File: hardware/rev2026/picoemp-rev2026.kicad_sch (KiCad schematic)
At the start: 53 parts, among them J1 EDGE-SMA, J2 1x2_Pin_Header, J3 MKDS 1,5/2-5.08, J4 EDGE-SMA, P1 Header 7, P2 Header 2, P3 Header 4, Q1 LDA111STR, Q2 RGT16BM65DTL, Q3 AO3422, Q4 AO3422, SW1 KSC741J LFS, SW2 KSC741J LFS, SW3 TL3301AF160QJ, T1 ATB322524, T2 ATB322524, U1 SC0915, U2 74LVC1G17

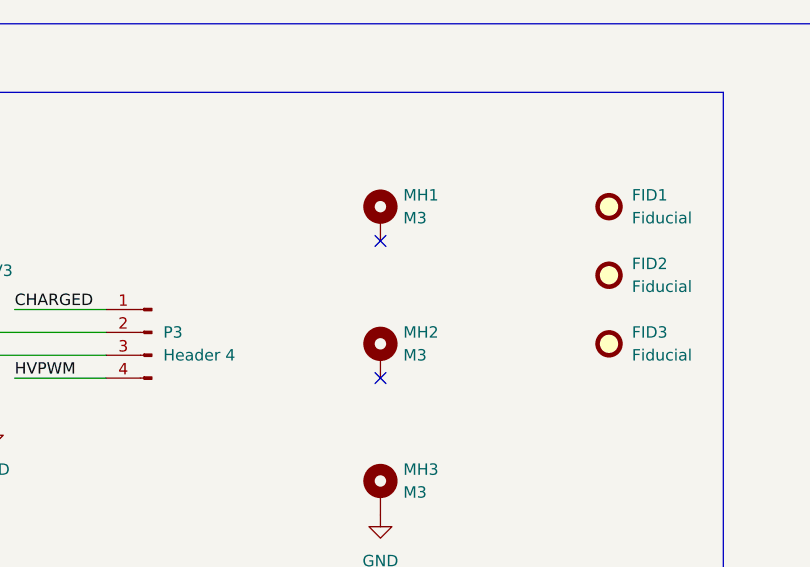
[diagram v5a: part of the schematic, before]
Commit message: MH1/MH2 to bare non-plated holes; HV_OUT reroute
MH1 and MH2 are now MountingHole_3.2mm_M3 as np_thru_hole -- no copper at all.
That removes two 6.4 mm floating pads from beside a 250 V node, and with them the
tightest barrier gap on the board: /HV_GATE was running 1.060 mm from MH1's pad.
The limit is now the transformers again at 1.135 mm. MH3 keeps its plated pad;
it sits at the logic end where floating copper is not a concern.

HV_OUT rerouted: 51.9 -> 22.2 mm. Discharge loop total 162.5 -> 131.5 mm.

Still open: one dangling via at (122.20, 147.20), B.Cu only, and J1's left shield
tab at (120.14, 147.2417) is not connected to copper. Electrically the shield is
one piece through the connector body, but DRC counts the islands.

Co-Authored-By: Claude Opus 5 <noreply@anthropic.com>
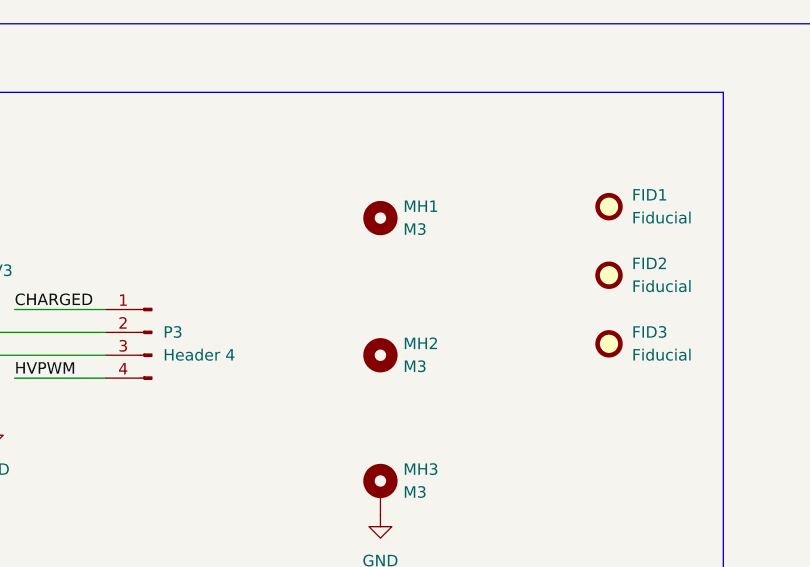
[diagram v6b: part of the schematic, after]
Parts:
- MH1, MH2: footprint MountingHole:MountingHole_3.2mm_M3_Pad_Via -> MountingHole:MountingHole_3.2mm_M3; symbol Mechanical:MountingHole_Pad -> Mechanical:MountingHole
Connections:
- no-connect marks 26 -> 24
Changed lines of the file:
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@@
 	)
 	(no_connect
-		(at 123.19 198.12)
-	)
-	(no_connect
 		(at 119.38 139.7)
 	)
 	(no_connect
-		(at 123.19 213.36)
-	)
-	(no_connect
 		(at 119.38 124.46)
 	)
@@
 	)
 	(symbol
-		(lib_id "Mechanical:MountingHole_Pad")
+		(lib_id "Mechanical:MountingHole")
 		(at 123.19 210.82 0)
 		(unit 1)
@@
 		(fields_autoplaced yes)
 		(property "Reference" "MH2"
-			(at 125.73 208.2799 0)
+			(at 125.73 209.5499 0)
 			(show_name no)
 			(do_not_autoplace no)
@@
 		)
 		(property "Value" "M3"
-			(at 125.73 210.8199 0)
+			(at 125.73 212.0899 0)
 			(show_name no)
 			(do_not_autoplace no)
@@
 			)
 		)
-		(property "Footprint" "MountingHole:MountingHole_3.2mm_M3_Pad_Via"
+		(property "Footprint" "MountingHole:MountingHole_3.2mm_M3"
 			(at 123.19 210.82 0)
 			(hide yes)
@@
 			)
 		)
-		(property "Description" "Mounting Hole with connection"
+		(property "Description" "Mounting Hole without connection"
 			(at 123.19 210.82 0)
 			(hide yes)
@@
 			)
 		)
-		(pin "1"
-		)
 		(instances
 			(project "picoemp-rev2026"
@@
 	)
 	(symbol
-		(lib_id "Mechanical:MountingHole_Pad")
+		(lib_id "Mechanical:MountingHole")
 		(at 123.19 195.58 0)
 		(unit 1)
@@
 		(fields_autoplaced yes)
 		(property "Reference" "MH1"
-			(at 125.73 193.0399 0)
+			(at 125.73 194.3099 0)
 			(show_name no)
 			(do_not_autoplace no)
@@
 		)
 		(property "Value" "M3"
-			(at 125.73 195.5799 0)
+			(at 125.73 196.8499 0)
 			(show_name no)
 			(do_not_autoplace no)
@@
 			)
 		)
-		(property "Footprint" "MountingHole:MountingHole_3.2mm_M3_Pad_Via"
+		(property "Footprint" "MountingHole:MountingHole_3.2mm_M3"
 			(at 123.19 195.58 0)
 			(hide yes)
@@
 			)
 		)
-		(property "Description" "Mounting Hole with connection"
+		(property "Description" "Mounting Hole without connection"
 			(at 123.19 195.58 0)
 			(hide yes)
@@
 			)
 		)
-		(pin "1"
-		)
 		(instances

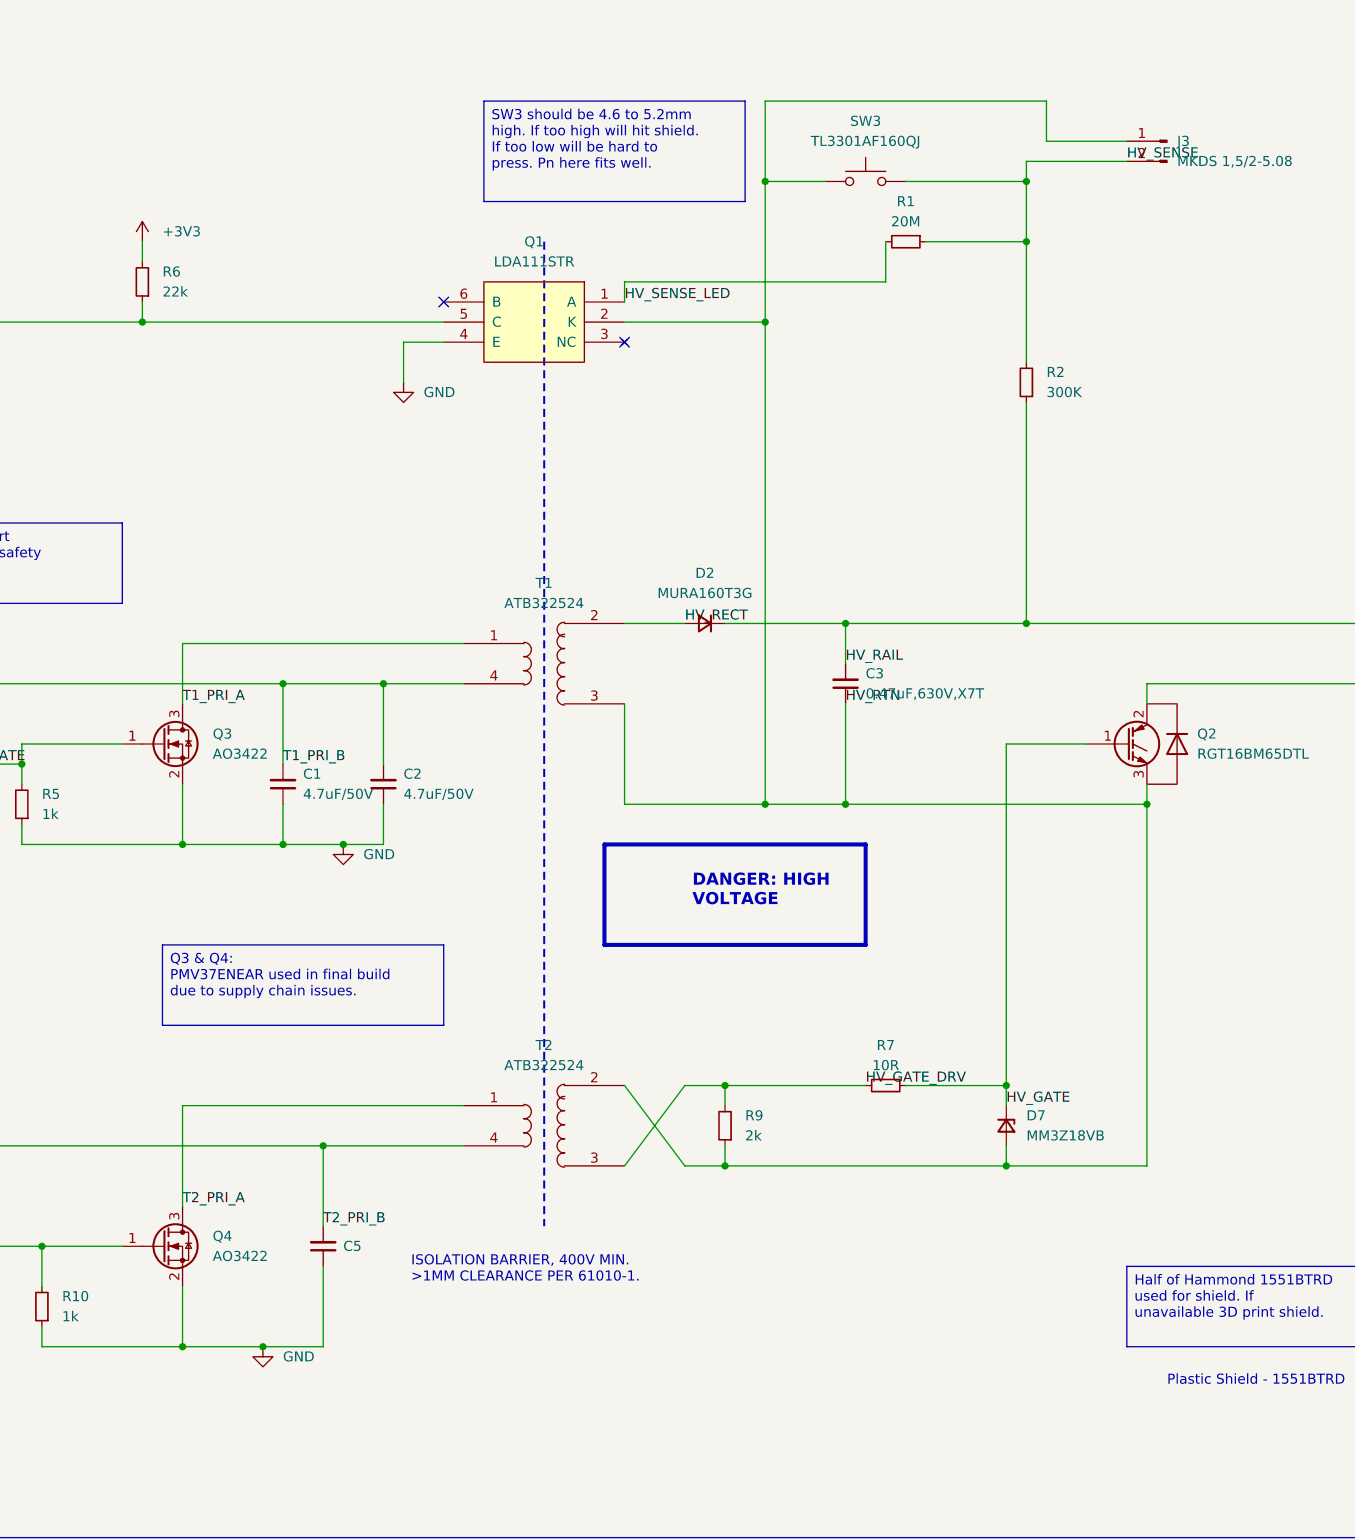
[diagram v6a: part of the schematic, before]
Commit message: Checkpoint: board origin shift, HV warning marks, intra-HV rule
Committing work that had been sitting uncommitted in the working tree, so the
1551G shield changes can be replayed on top of it without risking it.

  - whole board translated +25.400 mm in Y (X unchanged); origin was 19.872,
    now 45.272
  - two Symbol_HighVoltage_NoTriangle_2x5mm_Copper marks added at the board
    edges beside the HV section, (106.900,139.300) and (141.900,139.300),
    both carrying the unannotated reference REF**
  - .dru gains "Intra-HV spacing at full rail voltage": 0.8 mm, warning
    severity, scoped to the three pairs that genuinely stand at the rail --
    HV_RTN against HV_SENSE, HV_RAIL and HV_OUT. The barrier rule is
    HV-to-non-HV and says nothing about these.
  - schematic: 3 wires, 3 junctions and some repositioning; no component,
    value or property changes
  - LAYOUT-HANDOFF.md rewritten from instructions into a record

Gates at this commit: 66 tests pass; DRC with errors and warnings reports 0
violations, 0 unconnected, 0 footprint errors, exit 0. The new rule fires
correctly and finds nothing -- the header comment claiming 9 violations
predates the fixes that cleared them.

Co-Authored-By: Claude Opus 5 <noreply@anthropic.com>
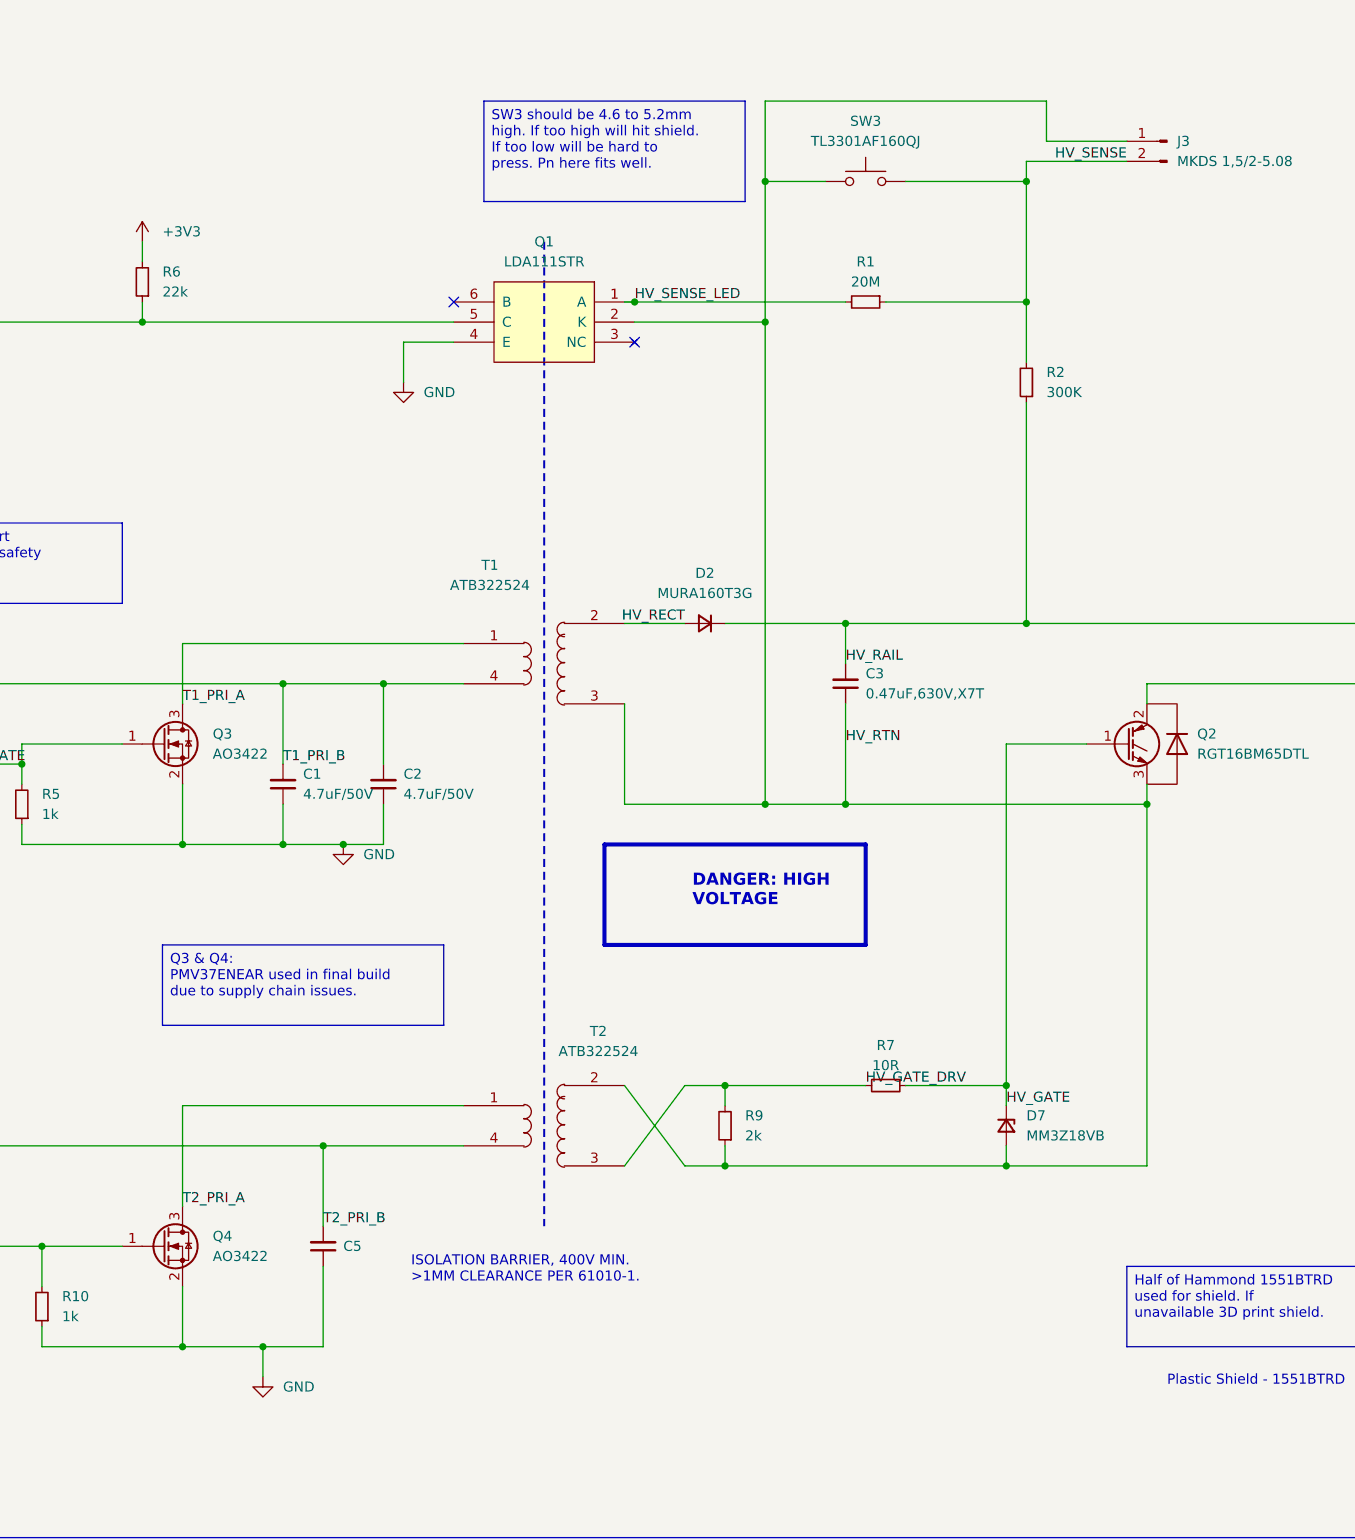
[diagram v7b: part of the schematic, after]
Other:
- moved on the sheet: Q1, R1
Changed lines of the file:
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@@
 	)
 	(junction
-		(at 256.54 238.76)
-		(diameter 0)
-		(color 0 0 0 0)
-	)
-	(junction
-		(at 368.3 228.6)
-		(diameter 0)
-		(color 0 0 0 0)
-	)
-	(junction
 		(at 241.3 294.64)
 		(diameter 0)
@@
 	)
 	(junction
-		(at 281.94 304.8)
+		(at 335.28 238.76)
 		(diameter 0)
 		(color 0 0 0 0)
 	)
 	(junction
-		(at 345.44 299.72)
+		(at 281.94 304.8)
 		(diameter 0)
 		(color 0 0 0 0)
@@
 	)
 	(junction
-		(at 271.78 368.3)
+		(at 256.54 238.76)
 		(diameter 0)
 		(color 0 0 0 0)
@@
 	)
 	(junction
+		(at 271.78 368.3)
+		(diameter 0)
+		(color 0 0 0 0)
+	)
+	(junction
+		(at 345.44 299.72)
+		(diameter 0)
+		(color 0 0 0 0)
+	)
+	(junction
 		(at 287.02 284.48)
 		(diameter 0)
@@
 	)
 	(junction
-		(at 335.28 238.76)
+		(at 368.3 236.22)
+		(diameter 0)
+		(color 0 0 0 0)
+	)
+	(junction
+		(at 318.77 236.22)
 		(diameter 0)
 		(color 0 0 0 0)
@@
 	)
 	(no_connect
-		(at 294.64 236.22)
+		(at 295.91 236.22)
 	)
 	(no_connect
@@
 	)
 	(no_connect
-		(at 317.5 241.3)
+		(at 318.77 241.3)
 	)
 	(no_connect
@@
 	(wire
 		(pts
-			(xy 368.3 220.98) (xy 368.3 228.6)
-		)
-		(stroke
-			(width 0)
-			(type default)
-		)
-	)
-	(wire
-		(pts
 			(xy 182.88 309.88) (xy 182.88 297.18)
 		)
@@
 	(wire
 		(pts
-			(xy 317.5 238.76) (xy 335.28 238.76)
+			(xy 318.77 238.76) (xy 335.28 238.76)
 		)
 		(stroke
@@
 	(wire
 		(pts
+			(xy 271.78 372.11) (xy 271.78 368.3)
+		)
+		(stroke
+			(width 0)
+			(type default)
+		)
+	)
+	(wire
+		(pts
 			(xy 193.04 309.88) (xy 200.66 309.88)
 		)
@@
 	(wire
 		(pts
-			(xy 368.3 228.6) (xy 368.3 243.84)
+			(xy 318.77 236.22) (xy 317.5 236.22)
 		)
 		(stroke
@@
 	(wire
 		(pts
-			(xy 345.44 299.72) (xy 345.44 287.02)
+			(xy 345.44 287.02) (xy 345.44 299.72)
 		)
 		(stroke
@@
 	(wire
 		(pts
-			(xy 294.64 241.3) (xy 289.56 241.3)
+			(xy 295.91 241.3) (xy 289.56 241.3)
 		)
 		(stroke
@@
 	(wire
 		(pts
-			(xy 317.5 233.68) (xy 317.5 236.22)
+			(xy 335.28 210.82) (xy 335.28 220.98)
 		)
 		(stroke
@@
 	(wire
 		(pts
-			(xy 335.28 210.82) (xy 335.28 220.98)
+			(xy 365.76 292.1) (xy 375.92 292.1)
 		)
 		(stroke
@@
 	(wire
 		(pts
-			(xy 365.76 292.1) (xy 375.92 292.1)
+			(xy 368.3 220.98) (xy 368.3 236.22)
 		)
 		(stroke
@@
 	(wire
 		(pts
-			(xy 355.6 228.6) (xy 368.3 228.6)
+			(xy 350.52 236.22) (xy 368.3 236.22)
 		)
 		(stroke
@@
 	(wire
 		(pts
-			(xy 256.54 238.76) (xy 294.64 238.76)
+			(xy 256.54 238.76) (xy 295.91 238.76)
 		)
 		(stroke
@@
 	(wire
 		(pts
+			(xy 318.77 236.22) (xy 345.44 236.22)
+		)
+		(stroke
+			(width 0)
+			(type default)
+		)
+	)
+	(wire
+		(pts
 			(xy 287.02 299.72) (xy 287.02 304.8)
 		)
@@
 	(wire
 		(pts
+			(xy 368.3 236.22) (xy 368.3 243.84)
+		)
+		(stroke
+			(width 0)
+			(type default)
+		)
+	)
+	(wire
+		(pts
 			(xy 35.56 205.74) (xy 53.34 205.74)
 		)
@@
 	(wire
 		(pts
-			(xy 317.5 233.68) (xy 350.52 233.68)
-		)
-		(stroke
-			(width 0)
-			(type default)
-		)
-	)
-	(wire
-		(pts
 			(xy 215.9 342.9) (xy 279.4 342.9)
 		)
@@
 	(wire
 		(pts
-			(xy 350.52 228.6) (xy 350.52 233.68)
-		)
-		(stroke
-			(width 0)
-			(type default)
-		)
-	)
-	(wire
-		(pts
 			(xy 279.4 342.9) (xy 279.4 353.06)
 		)
@@
 		)
 	)
+	(label "HV_SENSE_LED"
+		(at 318.77 236.22 0)
+		(effects
+			(font
+				(size 1.27 1.27)
+			)
+			(justify left bottom)
+		)
+	)
 	(label "HVPULSE"
 		(at 43.18 208.28 0)
@@
 		)
 	)
-	(label "HV_SENSE_LED"
-		(at 317.5 236.22 0)
-		(effects
-			(font
-				(size 1.27 1.27)
-			)
-			(justify left bottom)
-		)
-	)
 	(label "HV_SENSE"
-		(at 381 218.44 0)
+		(at 381 218.44 180)
 		(effects
 			(font
 				(size 1.27 1.27)
 			)
-			(justify left bottom)
+			(justify right bottom)
 		)
 	)
@@
 	)
 	(label "HV_RECT"
-		(at 325.12 276.86 0)
+		(at 325.12 276.86 180)
 		(effects
 			(font
 				(size 1.27 1.27)
 			)
-			(justify left bottom)
+			(justify right bottom)
 		)
 	)
@@
 	)
 	(label "HV_RTN"
-		(at 345.44 287.02 0)
+		(at 345.44 292.1 0)
 		(effects
 			(font
@@
 	(symbol
 		(lib_id "power:GND")
-		(at 271.78 368.3 0)
+		(at 271.78 372.11 0)
 		(unit 1)
 		(body_style 1)
@@
 		(fields_autoplaced yes)
 		(property "Reference" "#PWR03"
-			(at 271.78 368.3 0)
+			(at 271.78 372.11 0)
 			(hide yes)
 			(show_name no)
@@
 		)
 		(property "Value" "GND"
-			(at 274.32 369.5699 0)
+			(at 274.32 373.3799 0)
 			(show_name no)
 			(do_not_autoplace no)
@@
 		)
 		(property "Footprint" ""
-			(at 271.78 368.3 0)
+			(at 271.78 372.11 0)
 			(hide yes)
 			(show_name no)
@@
 		)
 		(property "Datasheet" ""
-			(at 271.78 368.3 0)
+			(at 271.78 372.11 0)
 			(hide yes)
 			(show_name no)
@@
 		)
 		(property "Description" "Power symbol creates a global label with name \"GND\" , ground"
-			(at 271.78 368.3 0)
+			(at 271.78 372.11 0)
 			(hide yes)
 			(show_name no)
@@
 		(in_pos_files yes)
 		(dnp no)
-		(fields_autoplaced yes)
 		(property "Reference" "T2"
-			(at 307.34 330.2 90)
+			(at 314.198 328.422 90)
 			(show_name no)
 			(do_not_autoplace no)
@@
 		)
 		(property "Value" "ATB322524"
-			(at 307.34 332.74 90)
+			(at 314.198 330.962 90)
 			(show_name no)
 			(do_not_autoplace no)
@@
 		(in_pos_files yes)
 		(dnp no)
-		(fields_autoplaced yes)
 		(property "Reference" "T1"
-			(at 307.34 271.78 90)
+			(at 300.482 269.494 90)
 			(show_name no)
 			(do_not_autoplace no)
@@
 		)
 		(property "Value" "ATB322524"
-			(at 307.34 274.32 90)
+			(at 300.482 272.034 90)
 			(show_name no)
 			(do_not_autoplace no)
@@
 	(symbol
 		(lib_id "Device:R_Small")
-		(at 353.06 228.6 270)
+		(at 347.98 236.22 270)
 		(unit 1)
 		(body_style 1)
@@
 		(fields_autoplaced yes)
 		(property "Reference" "R1"
-			(at 353.06 223.52 90)
+			(at 347.98 231.14 90)
 			(show_name no)
 			(do_not_autoplace no)
@@
 		)
 		(property "Value" "20M"
-			(at 353.06 226.06 90)
+			(at 347.98 233.68 90)
 			(show_name no)
 			(do_not_autoplace no)
@@
 		)
 		(property "Footprint" "Resistor_SMD:R_2010_5025Metric"
-			(at 353.06 228.6 0)
+			(at 347.98 236.22 0)
 			(hide yes)
 			(show_name no)
@@
 		)
 		(property "Datasheet" ""
-			(at 353.06 228.6 0)
+			(at 347.98 236.22 0)
 			(hide yes)
 			(show_name no)
@@
 		)
 		(property "Description" "Resistor, small symbol"
-			(at 353.06 228.6 0)
+			(at 347.98 236.22 0)
 			(hide yes)
 			(show_name no)
@@
 		)
 		(property "Manufacturer" "Vishay"
-			(at 352.044 234.188 0)
+			(at 346.964 241.808 0)
 			(hide yes)
 			(show_name no)
@@
 		)
 		(property "MPN" "CRMA2010AF20M0FKEF"
-			(at 352.044 234.188 0)
+			(at 346.964 241.808 0)
 			(hide yes)
 			(show_name no)
@@
 	(symbol
 		(lib_id "picoemp:LDA111")
-		(at 317.5 236.22 270)
+		(at 318.77 236.22 270)
 		(mirror x)
 		(unit 1)
@@
 		(fields_autoplaced yes)
 		(property "Reference" "Q1"
-			(at 306.07 228.6 90)
+			(at 307.34 228.6 90)
 			(show_name no)
 			(do_not_autoplace no)
@@
 		)
 		(property "Value" "LDA111STR"
-			(at 306.07 231.14 90)
+			(at 307.34 231.14 90)
 			(show_name no)
 			(do_not_autoplace no)
@@
 		)
 		(property "Footprint" "picoemp:SOP-6_LDA111"
-			(at 317.5 236.22 0)
+			(at 318.77 236.22 0)
 			(hide yes)
 			(show_name no)
@@
 		)
 		(property "Datasheet" ""
-			(at 317.5 236.22 0)
+			(at 318.77 236.22 0)
 			(hide yes)
 			(show_name no)
@@
 		)
 		(property "Description" "Phototransistor"
-			(at 317.5 236.22 0)
+			(at 318.77 236.22 0)
 			(hide yes)
 			(show_name no)
@@
 		)
 		(property "Manufacturer" "IXYS SEMICONDUCTOR"
-			(at 294.132 233.68 90)
+			(at 295.402 233.68 90)
 			(hide yes)
 			(show_name no)
@@
 		)
 		(property "MPN" "LDA111STR"
-			(at 294.132 233.68 90)
+			(at 295.402 233.68 90)
 			(hide yes)
 			(show_name no)
@@
 		)
 		(property "DigiKey" "212-LDA111SCT-ND"
-			(at 0 0 0)
+			(at 1.27 0 0)
 			(hide yes)
 			(show_name no)
